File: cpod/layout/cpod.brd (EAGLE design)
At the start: 61 x 43.2 mm, 9 parts

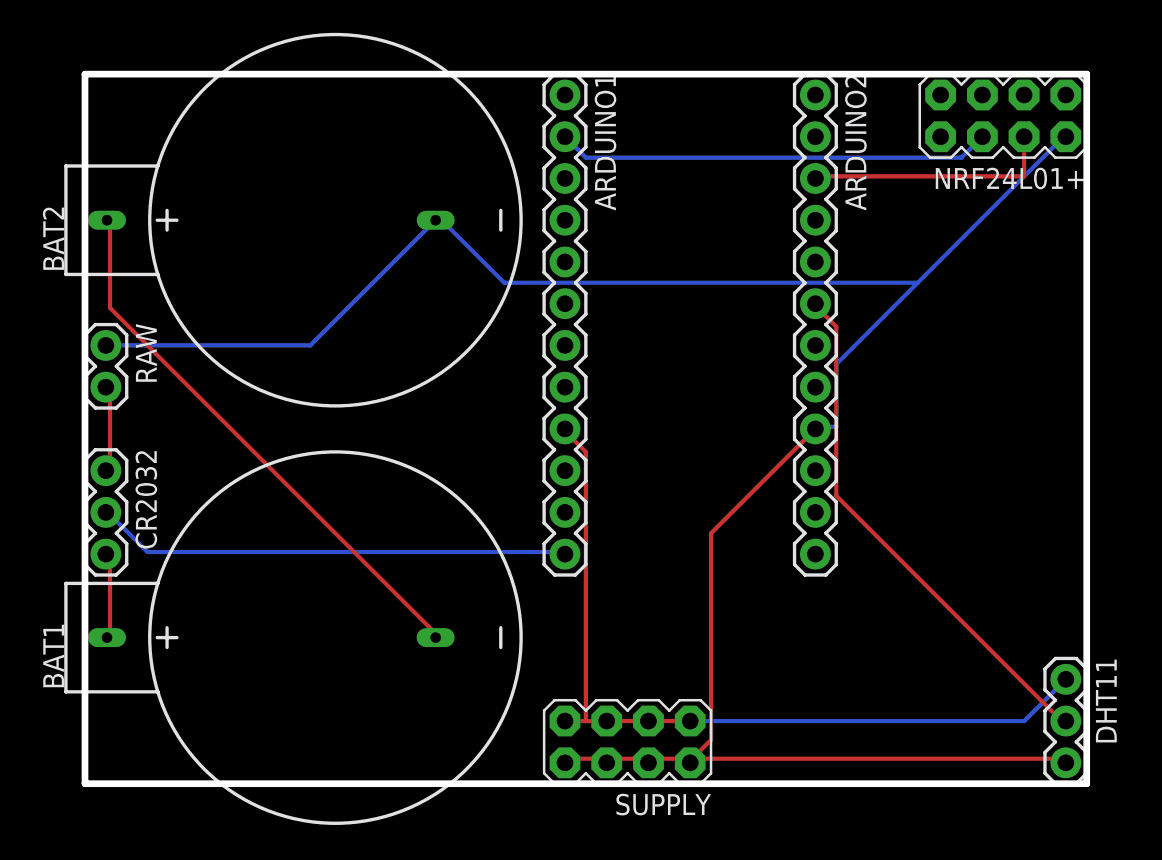
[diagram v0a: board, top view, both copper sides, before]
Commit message: NRF24L01+下调一格
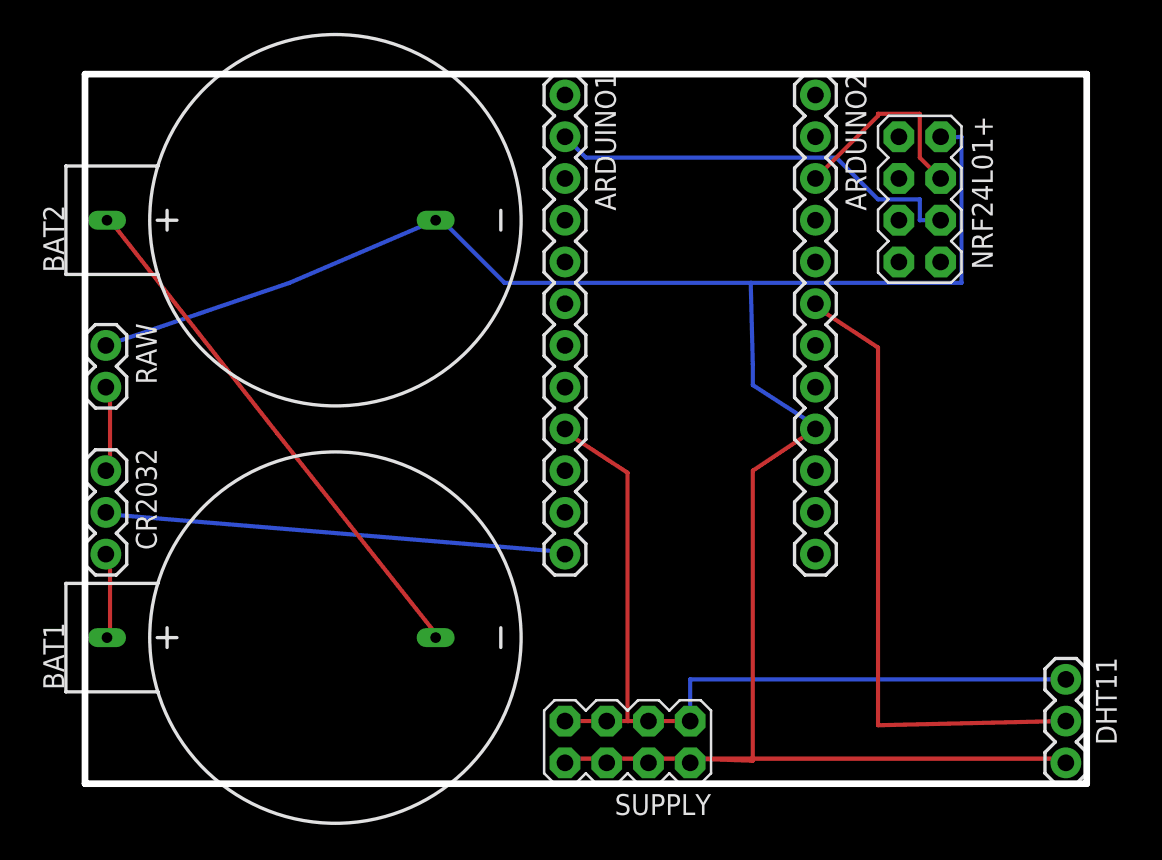
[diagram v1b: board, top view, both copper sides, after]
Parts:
- moved NRF24L01+ 7.18 mm to (50.8, 35.6), turned to 270 degrees
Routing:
- net D4: track 31.8 -> 39.1 mm
- net VCC: track 49.8 -> 52.8 mm
- net CSN: track 15.2 -> 12.5 mm
- net N$1: track 33.8 -> 32.5 mm
- net MOSI: track 26.5 -> 25.7 mm
- net GND: track 133.6 -> 134.3 mm
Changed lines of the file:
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@@
 <element name="CR2032" library="SparkFun-Connectors" package="1X03" value="" x="1.27" y="19.05" rot="R270"/>
 <element name="SUPPLY" library="SparkFun-Connectors" package="2X4" value="M04X2" x="33.02" y="2.54" rot="R180"/>
-<element name="NRF24L01+" library="SparkFun-Connectors" package="2X4" value="M04X2" x="55.88" y="40.64" rot="R180"/>
+<element name="NRF24L01+" library="SparkFun-Connectors" package="2X4" value="M04X2" x="50.8" y="35.56" rot="R270"/>
 <element name="RAW" library="SparkFun-Connectors" package="1X02" value="" x="1.27" y="26.67" rot="R270"/>
 <element name="DHT11" library="SparkFun-Connectors" package="1X03" value="" x="59.69" y="6.35" rot="R270"/>
@@
 <contactref element="SUPPLY" pad="8"/>
 <contactref element="RAW" pad="1"/>
-<wire x1="13.716" y1="26.67" x2="21.336" y2="34.29" width="0.254" layer="16"/>
-<wire x1="1.27" y1="26.67" x2="13.716" y2="26.67" width="0.254" layer="16"/>
+<wire x1="12.446" y1="30.48" x2="21.336" y2="34.29" width="0.254" layer="16"/>
+<wire x1="1.27" y1="26.67" x2="12.446" y2="30.48" width="0.254" layer="16"/>
 <wire x1="21.336" y1="34.29" x2="21.34" y2="34.29" width="0.254" layer="16"/>
 <wire x1="31.623" y1="1.524" x2="29.337" y2="1.524" width="0.254" layer="1"/>
@@
 <wire x1="36.576" y1="1.524" x2="36.83" y2="1.27" width="0.254" layer="1"/>
 <wire x1="34.29" y1="1.524" x2="34.29" y2="1.27" width="0.254" layer="1"/>
-<wire x1="38.1" y1="15.24" x2="44.45" y2="21.59" width="0.254" layer="1"/>
-<wire x1="38.1" y1="2.667" x2="38.1" y2="15.24" width="0.254" layer="1"/>
-<wire x1="36.957" y1="1.524" x2="38.1" y2="2.667" width="0.254" layer="1"/>
+<wire x1="40.64" y1="19.05" x2="44.45" y2="21.59" width="0.254" layer="1"/>
+<wire x1="40.64" y1="1.397" x2="40.64" y2="19.05" width="0.254" layer="1"/>
+<wire x1="36.957" y1="1.524" x2="40.64" y2="1.397" width="0.254" layer="1"/>
 <wire x1="36.957" y1="1.524" x2="59.436" y2="1.524" width="0.254" layer="1"/>
 <wire x1="59.436" y1="1.524" x2="59.69" y2="1.27" width="0.254" layer="1"/>
 <wire x1="36.957" y1="1.524" x2="36.83" y2="1.27" width="0.254" layer="1"/>
-<wire x1="45.72" y1="25.527" x2="50.673" y2="30.48" width="0.254" layer="16"/>
-<wire x1="50.673" y1="30.48" x2="59.436" y2="39.243" width="0.254" layer="16"/>
-<wire x1="45.72" y1="21.717" x2="45.72" y2="25.527" width="0.254" layer="16"/>
-<wire x1="44.577" y1="21.717" x2="45.72" y2="21.717" width="0.254" layer="16"/>
-<wire x1="59.436" y1="39.243" x2="59.69" y2="39.37" width="0.254" layer="16"/>
+<wire x1="40.64" y1="25.527" x2="40.513" y2="30.48" width="0.254" layer="16"/>
+<wire x1="40.513" y1="30.48" x2="53.34" y2="30.48" width="0.254" layer="16"/>
+<wire x1="53.34" y1="30.48" x2="53.34" y2="39.37" width="0.254" layer="16"/>
+<wire x1="53.34" y1="39.37" x2="51.816" y2="39.243" width="0.254" layer="16"/>
+<wire x1="40.64" y1="24.257" x2="40.64" y2="25.527" width="0.254" layer="16"/>
+<wire x1="44.577" y1="21.717" x2="40.64" y2="24.257" width="0.254" layer="16"/>
+<wire x1="51.816" y1="39.243" x2="52.07" y2="39.37" width="0.254" layer="16"/>
 <wire x1="44.577" y1="21.717" x2="44.45" y2="21.59" width="0.254" layer="16"/>
 <wire x1="25.527" y1="30.48" x2="21.717" y2="34.29" width="0.254" layer="16"/>
-<wire x1="50.673" y1="30.48" x2="25.527" y2="30.48" width="0.254" layer="16"/>
+<wire x1="40.513" y1="30.48" x2="25.527" y2="30.48" width="0.254" layer="16"/>
 <wire x1="21.717" y1="34.29" x2="21.34" y2="34.29" width="0.254" layer="16"/>
 </signal>
@@
 <contactref element="ARDUINO1" pad="12"/>
 <contactref element="CR2032" pad="2"/>
-<wire x1="3.81" y1="14.097" x2="1.524" y2="16.383" width="0.254" layer="16"/>
-<wire x1="28.956" y1="14.097" x2="3.81" y2="14.097" width="0.254" layer="16"/>
+<wire x1="29.21" y1="14.097" x2="1.524" y2="16.383" width="0.254" layer="16"/>
+<wire x1="28.956" y1="14.097" x2="29.21" y2="14.097" width="0.254" layer="16"/>
 <wire x1="1.524" y1="16.383" x2="1.27" y2="16.51" width="0.254" layer="16"/>
 <wire x1="28.956" y1="14.097" x2="29.21" y2="13.97" width="0.254" layer="16"/>
@@
 <contactref element="ARDUINO1" pad="4"/>
 <contactref element="NRF24L01+" pad="5"/>
-<wire x1="29.21" y1="34.29" x2="54.61" y2="41.91" width="0" layer="19" extent="1-1"/>
+<wire x1="29.21" y1="34.29" x2="49.53" y2="34.29" width="0" layer="19" extent="1-1"/>
 </signal>
 <signal name="AD0">
@@
 <contactref element="ARDUINO2" pad="6"/>
 <contactref element="DHT11" pad="2"/>
-<wire x1="45.72" y1="17.526" x2="59.436" y2="3.81" width="0.254" layer="1"/>
-<wire x1="45.72" y1="27.813" x2="45.72" y2="17.526" width="0.254" layer="1"/>
-<wire x1="44.577" y1="28.956" x2="45.72" y2="27.813" width="0.254" layer="1"/>
+<wire x1="48.26" y1="3.556" x2="59.436" y2="3.81" width="0.254" layer="1"/>
+<wire x1="48.26" y1="26.543" x2="48.26" y2="3.556" width="0.254" layer="1"/>
+<wire x1="44.577" y1="28.956" x2="48.26" y2="26.543" width="0.254" layer="1"/>
 <wire x1="59.436" y1="3.81" x2="59.69" y2="3.81" width="0.254" layer="1"/>
 <wire x1="44.577" y1="28.956" x2="44.45" y2="29.21" width="0.254" layer="1"/>
@@
 <contactref element="NRF24L01+" pad="3"/>
 <contactref element="ARDUINO2" pad="2"/>
-<wire x1="44.45" y1="39.37" x2="57.15" y2="41.91" width="0" layer="19" extent="1-1"/>
+<wire x1="44.45" y1="39.37" x2="49.53" y2="36.83" width="0" layer="19" extent="1-1"/>
 </signal>
 <signal name="MISO">
 <contactref element="NRF24L01+" pad="7"/>
 <contactref element="ARDUINO1" pad="3"/>
-<wire x1="29.21" y1="36.83" x2="52.07" y2="41.91" width="0" layer="19" extent="1-1"/>
+<wire x1="29.21" y1="36.83" x2="49.53" y2="31.75" width="0" layer="19" extent="1-1"/>
 </signal>
 <signal name="CSN">
 <contactref element="NRF24L01+" pad="4"/>
 <contactref element="ARDUINO2" pad="3"/>
-<wire x1="57.15" y1="36.957" x2="44.577" y2="36.957" width="0.254" layer="1"/>
-<wire x1="57.15" y1="39.37" x2="57.15" y2="36.957" width="0.254" layer="1"/>
-<wire x1="44.577" y1="36.957" x2="44.45" y2="36.83" width="0.254" layer="1"/>
+<wire x1="48.26" y1="40.767" x2="48.26" y2="40.64" width="0.254" layer="1"/>
+<wire x1="48.26" y1="40.64" x2="44.45" y2="36.83" width="0.254" layer="1"/>
+<wire x1="52.07" y1="36.83" x2="50.8" y2="38.1" width="0.254" layer="1"/>
+<wire x1="50.8" y1="38.1" x2="50.8" y2="40.767" width="0.254" layer="1"/>
+<wire x1="50.8" y1="40.767" x2="48.26" y2="40.767" width="0.254" layer="1"/>
 </signal>
 <signal name="MOSI">
@@
 <contactref element="ARDUINO1" pad="2"/>
 <wire x1="30.48" y1="38.1" x2="29.21" y2="39.37" width="0.254" layer="16"/>
-<wire x1="53.34" y1="38.1" x2="30.48" y2="38.1" width="0.254" layer="16"/>
-<wire x1="54.61" y1="39.37" x2="53.34" y2="38.1" width="0.254" layer="16"/>
+<wire x1="45.72" y1="38.1" x2="30.48" y2="38.1" width="0.254" layer="16"/>
+<wire x1="52.07" y1="34.29" x2="50.8" y2="34.29" width="0.254" layer="16"/>
+<wire x1="50.8" y1="34.29" x2="50.8" y2="35.56" width="0.254" layer="16"/>
+<wire x1="50.8" y1="35.56" x2="48.26" y2="35.56" width="0.254" layer="16"/>
+<wire x1="48.26" y1="35.56" x2="45.72" y2="38.1" width="0.254" layer="16"/>
 </signal>
 <signal name="IRQ">
@@
 <contactref element="SUPPLY" pad="5"/>
 <contactref element="SUPPLY" pad="7"/>
-<wire x1="31.75" y1="3.81" x2="30.48" y2="3.81" width="0.254" layer="1"/>
-<wire x1="30.48" y1="3.81" x2="29.21" y2="3.81" width="0.254" layer="1"/>
-<wire x1="31.75" y1="3.81" x2="34.29" y2="3.81" width="0.254" layer="1"/>
+<wire x1="33.02" y1="3.81" x2="29.21" y2="3.81" width="0.254" layer="1"/>
+<wire x1="33.02" y1="3.81" x2="34.29" y2="3.81" width="0.254" layer="1"/>
 <wire x1="34.29" y1="3.81" x2="36.83" y2="3.81" width="0.254" layer="1"/>
-<wire x1="30.48" y1="20.193" x2="29.337" y2="21.336" width="0.254" layer="1"/>
-<wire x1="30.48" y1="3.81" x2="30.48" y2="20.193" width="0.254" layer="1"/>
+<wire x1="33.02" y1="18.923" x2="29.337" y2="21.336" width="0.254" layer="1"/>
+<wire x1="33.02" y1="3.81" x2="33.02" y2="18.923" width="0.254" layer="1"/>
 <wire x1="29.337" y1="21.336" x2="29.21" y2="21.59" width="0.254" layer="1"/>
-<wire x1="57.15" y1="3.81" x2="59.69" y2="6.35" width="0.254" layer="16"/>
-<wire x1="36.83" y1="3.81" x2="57.15" y2="3.81" width="0.254" layer="16"/>
-<wire x1="59.69" y1="6.35" x2="59.69" y2="41.91" width="0" layer="19" extent="1-1"/>
+<wire x1="36.83" y1="6.35" x2="59.69" y2="6.35" width="0.254" layer="16"/>
+<wire x1="36.83" y1="3.81" x2="36.83" y2="6.35" width="0.254" layer="16"/>
+<wire x1="29.21" y1="21.59" x2="49.53" y2="39.37" width="0" layer="19" extent="1-1"/>
 </signal>
 <signal name="N$1">
 <contactref element="BAT1" pad="-"/>
 <contactref element="BAT2" pad="+"/>
-<wire x1="1.524" y1="28.956" x2="21.336" y2="9.144" width="0.254" layer="1"/>
-<wire x1="1.524" y1="34.29" x2="1.524" y2="28.956" width="0.254" layer="1"/>
+<wire x1="11.684" y1="21.336" x2="21.336" y2="9.144" width="0.254" layer="1"/>
+<wire x1="1.524" y1="34.29" x2="11.684" y2="21.336" width="0.254" layer="1"/>
 <wire x1="21.336" y1="9.144" x2="21.34" y2="8.89" width="0.254" layer="1"/>
 <wire x1="1.524" y1="34.29" x2="1.34" y2="34.29" width="0.254" layer="1"/>
